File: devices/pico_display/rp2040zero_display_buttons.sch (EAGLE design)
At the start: 14 parts, among them U1 RP2040-ZERO'

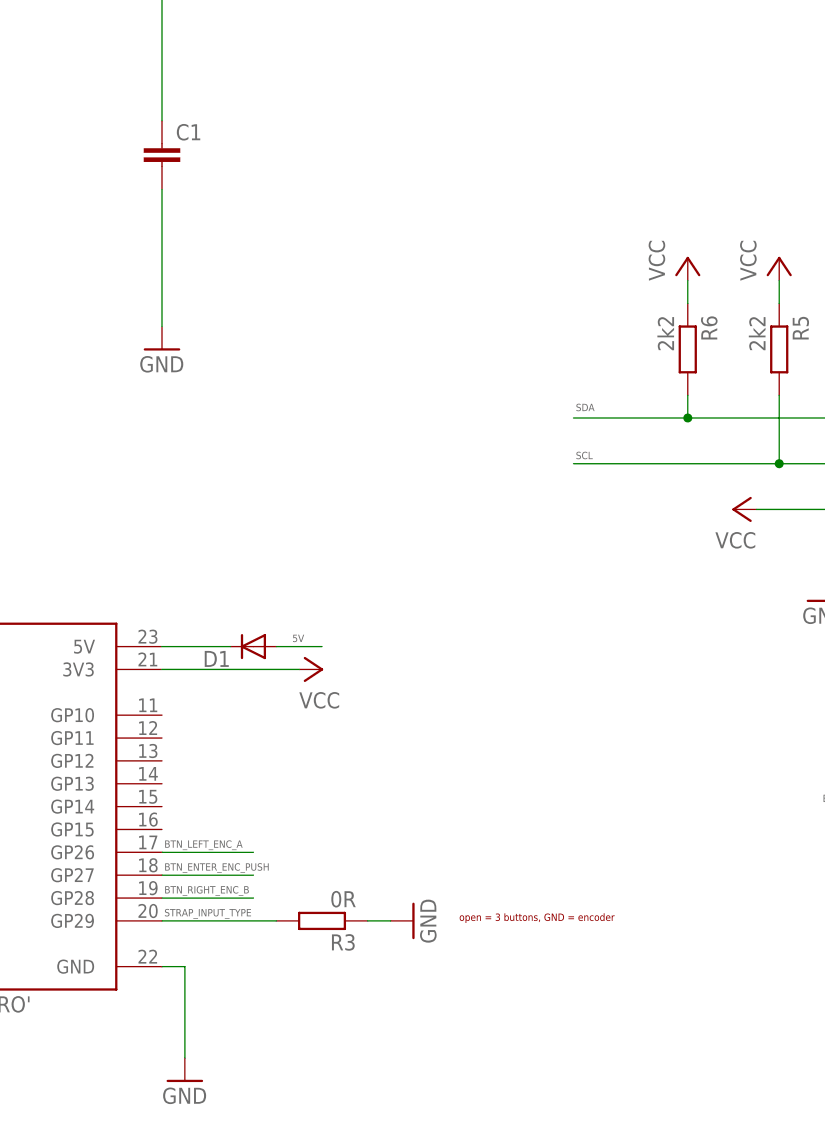
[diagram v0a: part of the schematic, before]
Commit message: fixes to display sch and brd
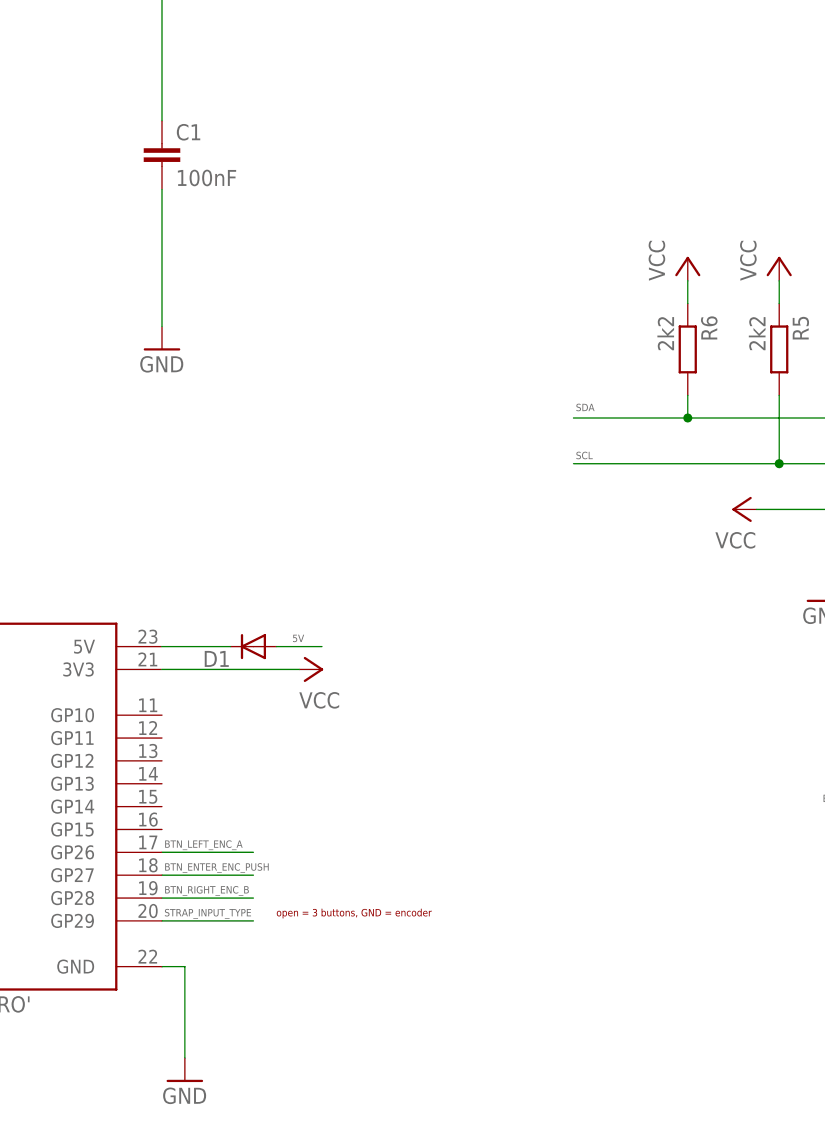
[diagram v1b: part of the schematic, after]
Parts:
- removed R3: 0R, resistor:R-EU_R0603
- C1: value (none) -> 100nF
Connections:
- net GND: no longer R3.1
- net STRAP_INPUT_TYPE: no longer R3.2
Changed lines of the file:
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@@
 <part name="D1" library="diode" deviceset="DIODE-" device="DO214AC" value="SK110-DIO"/>
 <part name="GND2" library="supply1" deviceset="GND" device=""/>
-<part name="R3" library="resistor" deviceset="R-EU_" device="R0603" value="0R"/>
-<part name="GND3" library="supply1" deviceset="GND" device=""/>
 <part name="S1" library="DTSM-62N-V-B" deviceset="DTSM-62N-V-B" device=""/>
 <part name="S2" library="DTSM-62N-V-B" deviceset="DTSM-62N-V-B" device=""/>
@@
 <part name="P+22" library="supply1" deviceset="VCC" device=""/>
 <part name="P+1" library="supply1" deviceset="VCC" device=""/>
-<part name="C1" library="rcl" deviceset="C-EU" device="C0603"/>
+<part name="C1" library="rcl" deviceset="C-EU" device="C0603" value="100nF"/>
 <part name="R5" library="resistor" deviceset="R-EU_" device="R0603" value="2k2"/>
 <part name="R6" library="resistor" deviceset="R-EU_" device="R0603" value="2k2"/>
@@
 <wire x1="25.4" y1="41.656" x2="25.4" y2="41.148" width="0.1524" layer="94"/>
 <wire x1="25.4" y1="41.148" x2="24.384" y2="41.402" width="0.1524" layer="94"/>
-<text x="124.46" y="17.78" size="0.8128" layer="94" font="vector">open = 3 buttons, GND = encoder</text>
+<text x="104.14" y="18.288" size="0.8128" layer="94" font="vector">open = 3 buttons, GND = encoder</text>
 </plain>
 <instances>
@@
 </instance>
 <instance part="GND2" gate="1" x="93.98" y="0"/>
-<instance part="R3" gate="G$1" x="109.22" y="17.78" rot="R180"/>
-<instance part="GND3" gate="1" x="119.38" y="17.78" rot="R90"/>
 <instance part="S1" gate="G$1" x="172.72" y="25.4" rot="R270"/>
 <instance part="S2" gate="G$1" x="190.5" y="25.4" rot="R270"/>
@@
 </segment>
 <segment>
-<pinref part="R3" gate="G$1" pin="1"/>
-<pinref part="GND3" gate="1" pin="GND"/>
-<wire x1="114.3" y1="17.78" x2="116.84" y2="17.78" width="0.1524" layer="91"/>
-</segment>
-<segment>
 <pinref part="S1" gate="G$1" pin="NO_2"/>
 <pinref part="GND5" gate="1" pin="GND"/>
@@
 <segment>
 <pinref part="U1" gate="G$1" pin="GP29"/>
-<wire x1="91.44" y1="17.78" x2="104.14" y2="17.78" width="0.1524" layer="91"/>
+<wire x1="91.44" y1="17.78" x2="101.6" y2="17.78" width="0.1524" layer="91"/>
 <label x="91.694" y="18.288" size="0.8128" layer="95" font="vector"/>
-<pinref part="R3" gate="G$1" pin="2"/>
-</segment>
-</net>
+</segment>
+</net>
